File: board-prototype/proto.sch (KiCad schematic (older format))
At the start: 66 parts, among them P1 AB, P101 Data, P102 Power, P2 CD, SW101 RESET, U101 Am2908, U102 Am2908, U103 Am2908, U104 Am2908, U105 Am2908, U106 Am2908, U107 74LVC7T245, U108 74LVC7T245, U109 74LVC7T245, U110 MAX3488, U111 MAX3488, U112 MAX3488, U115 74LVC7T245, U116 74LVC7T245, U117 74LVC7T245, U118 74LVC7T245, U119 74LVC7T245, U120 LD1117S33CTR, U201 DS8641-LR, U202 DS8641-LR, U203 DS8641-LR, U204 DS8641-LR, U205 DS8641-LR

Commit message: Split schematic into multiple sheets.
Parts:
- removed P1: AB, Pin_Headers:Pin_Header_Straight_2x32, symbol CONN_ZTEX_AB
- removed P101: Data, Pin_Headers:Pin_Header_Angled_2x04, symbol CONN_02X04
- removed P102: Power, Pin_Headers:Pin_Header_Angled_2x05, symbol CONN_02X05
- removed P2: CD, Pin_Headers:Pin_Header_Straight_2x32, symbol CONN_ZTEX_CD
- removed R101, R103, R105, R107: 330Ω, Resistors_SMD:R_0805, symbol R
- removed R102, R104, R106, R108: 680Ω, Resistors_SMD:R_0805, symbol R
- removed SW101: RESET, symbol SW_PUSH_SMALL
- removed U101, U102, U103, U104, U105, U106: Am2908, Sockets_DIP:DIP-20__300, symbol Am2908
- removed U107, U108, U109, U115, U116, U117, U118, U119: 74LVC7T245, SMD_Packages:SOIC-24, symbol 74LVC7T245
- removed U110, U111, U112: MAX3488, Housings_DIP:DIP-8__300, symbol MAX3488
- removed U201, U202, U203, U204, U205: DS8641-LR, Sockets_DIP:DIP-16__300, symbol DS8641-LR
- added C122, C123, C124: 100nF, Capacitors_SMD:C_0805, symbol C_Small
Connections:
- net +3V3: now also C122.1, C123.1, C124.1
- net GND: now also C122.2, C123.2, C124.2
- net BHALT: now reaches B101.AP1 (BHALT)
- no-connect marks 83 -> 14
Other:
- note removed: "Indicator Panel"
- note removed: "NOTES:\n\n1) Which signal goes to which package has not yet\n been fixed. Will be done during PCB layout.\n2) Do we need to tie the unconnected bus lines on\n the DS8641s to +5V?\n3) Check that Vcc to the RS422 drivers is the right\n voltage."
- note removed: "ZTEX Module Connector"
- moved on the sheet: B101, C101, C102, C103, C104, C105, C106, C107, C108, C109, C110, C111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

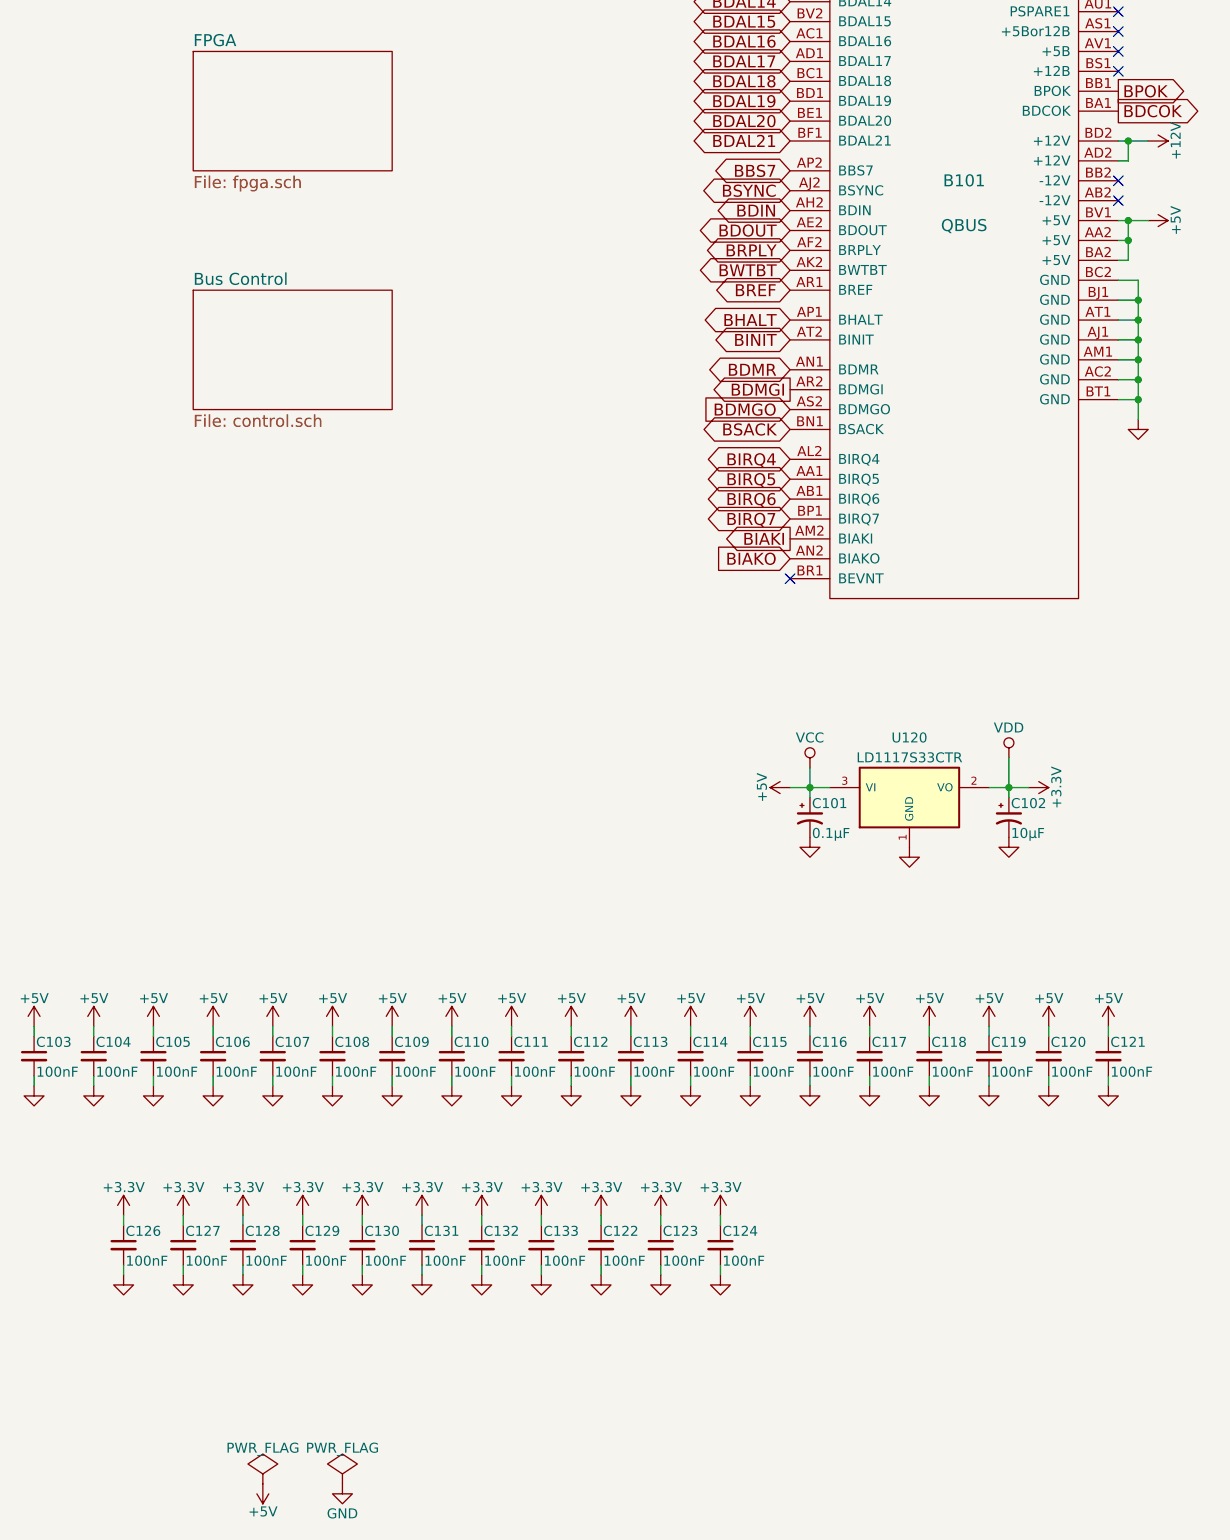
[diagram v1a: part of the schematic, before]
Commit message: Changed over to only DS8641 bus transceivers and the smaller package level-converters.
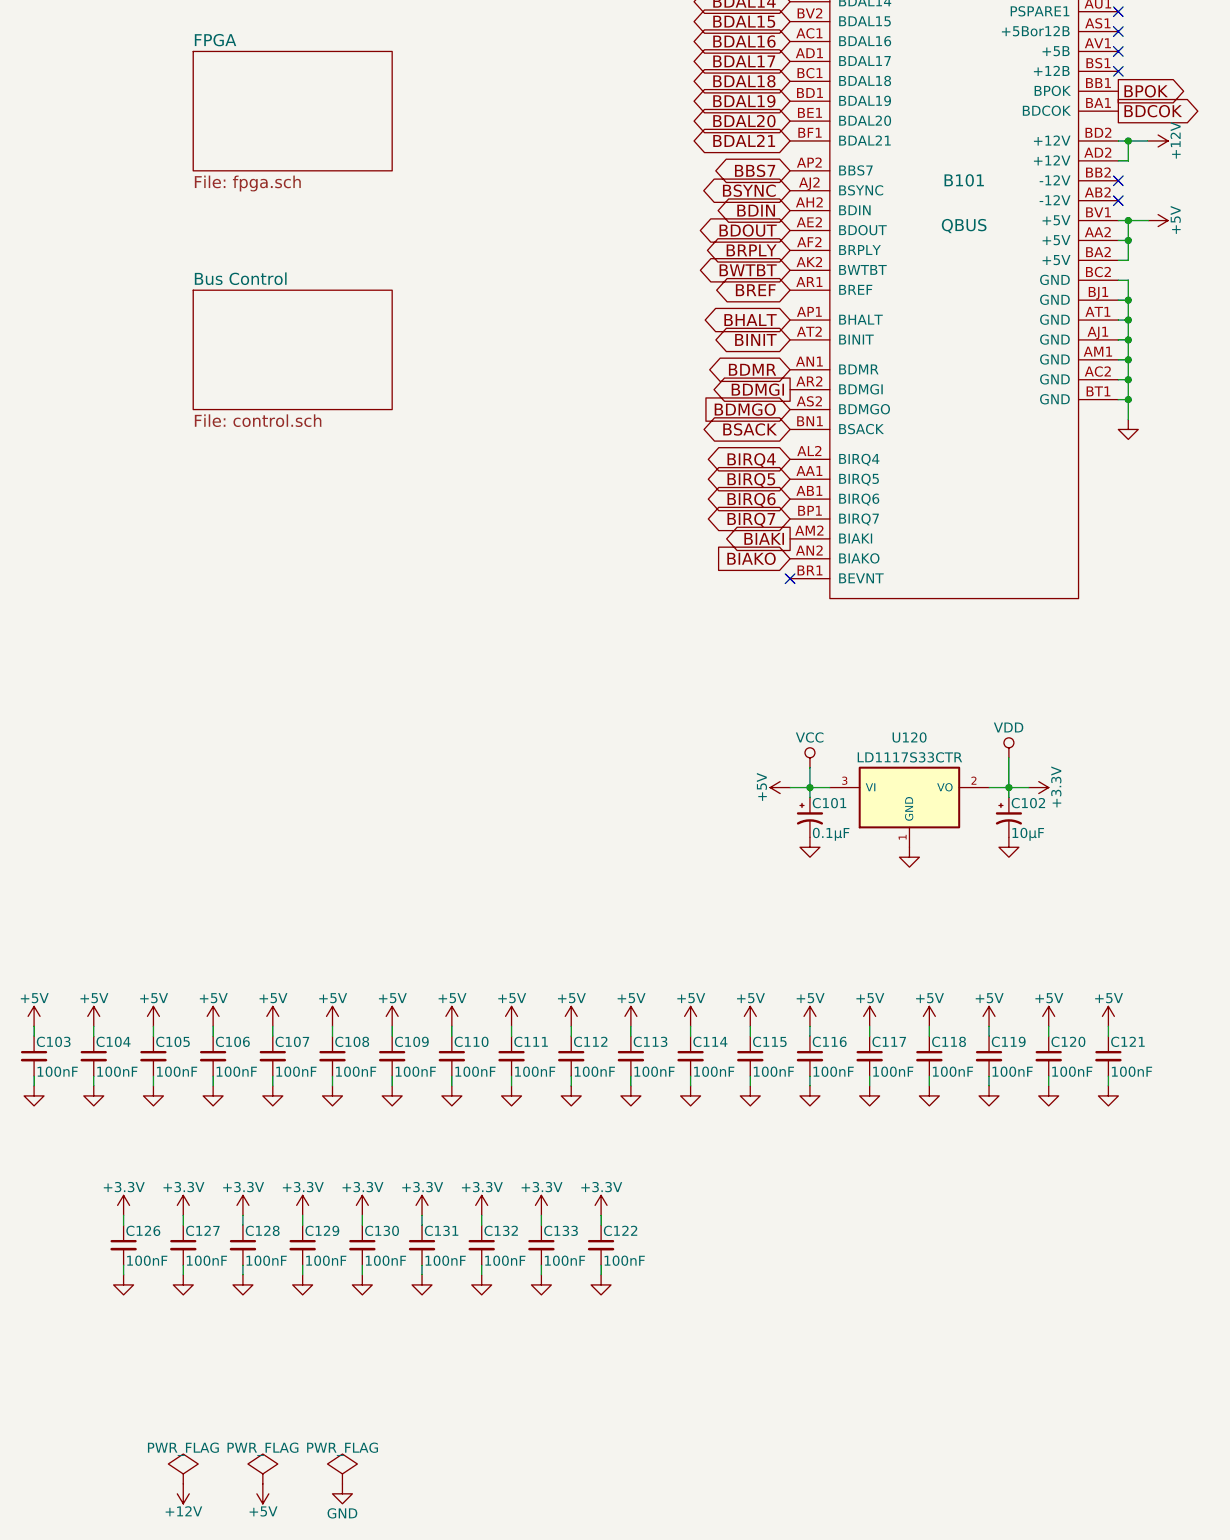
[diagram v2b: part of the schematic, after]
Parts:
- removed C123, C124: 100nF, Capacitors_SMD:C_0805, symbol C_Small
- B101: footprint myMods.pretty:Qbus -> myMods.pretty:Qbus-double

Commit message: Updated to KiCad 5
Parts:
- B101: symbol QBUS -> myLib:QBUS
- C101, C102: symbol CP1_Small -> device:CP1_Small
- C103, C104, C105, C106, C107, C108, C109, C110, C111, C112, C113, C114, C115, C116, C117, C118, C119, C120, C121, C122, C126, C127, C128, C129, C130, C131, C132, C133: symbol C_Small -> device:C_Small
- U120: symbol LD1117S33CTR -> regul:LD1117S33CTR
